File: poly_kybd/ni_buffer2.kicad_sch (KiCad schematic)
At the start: 2 parts, among them U12 SN74LVC1G126DBVR, U13 SN74LVC1G126DBVR

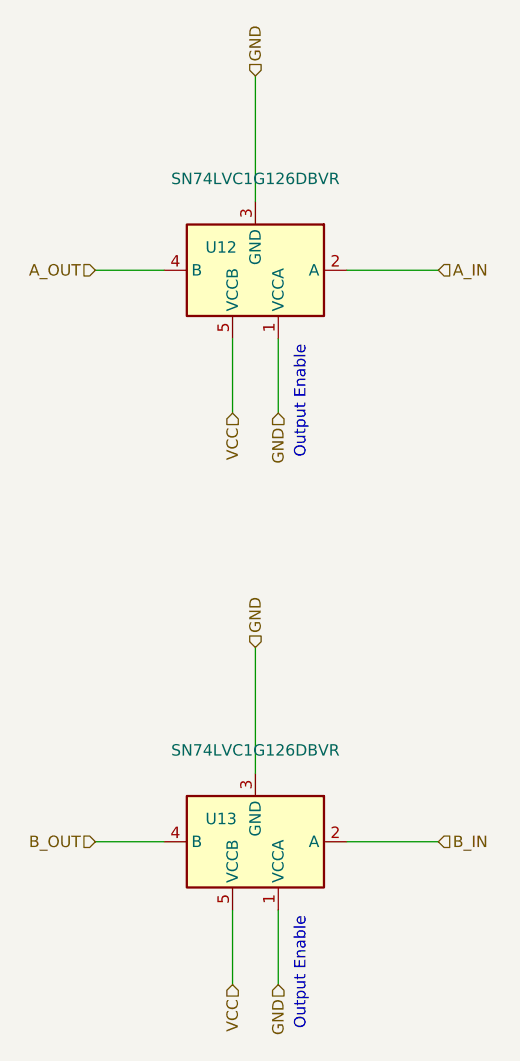
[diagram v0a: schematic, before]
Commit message: v3.3: replace SN74LVC1G126 buffer symbol with Nexperia 74AHC1G125
U12/U13 in ni_buffer2.kicad_sch were drawn with the
Logic_LevelTranslator:SN74AUP1T34DCK symbol, which mislabels pins 1 and 5
as VCCA/VCCB. The fitted part is a single-gate tri-state buffer, where
pin 1 is /OE and pin 5 is VCC.

Pin *numbers* drive the netlist and those were always right, so the built
v3.2 boards are electrically correct. This is a drawing fix - it matters
because the schematic is exported into the CE technical file.

- swap to 74xGxx:74AHC1G125, rev v3.3
- retarget U12/U13 to Nexperia 74AHC1G125GW,125 (LCSC C85397); the
  previously specified part is EOL at JLCPCB
- reroute the wires: the new symbol has different pin geometry, so all
  ten pins had to be reconnected. Net assignment verified unchanged -
  /OE and GND to GND, A to A_IN/B_IN, Y to A_OUT/B_OUT, VCC to VCC
- delete ni_buffer.kicad_sch and mini-360.kicad_sch, neither instantiated
  by any sheet

poly_kybd_split72_left.kicad_sch was rewritten from KiCad 8 to 9 format
on open. Verified harmless: all 186 symbol pins sit at identical
coordinates before and after. Note this is one-way - KiCad 8 can no
longer open the project.

The PCB still carries the old footprint value; Update PCB from Schematic
is the next step.

Co-Authored-By: Claude Opus 5 <noreply@anthropic.com>
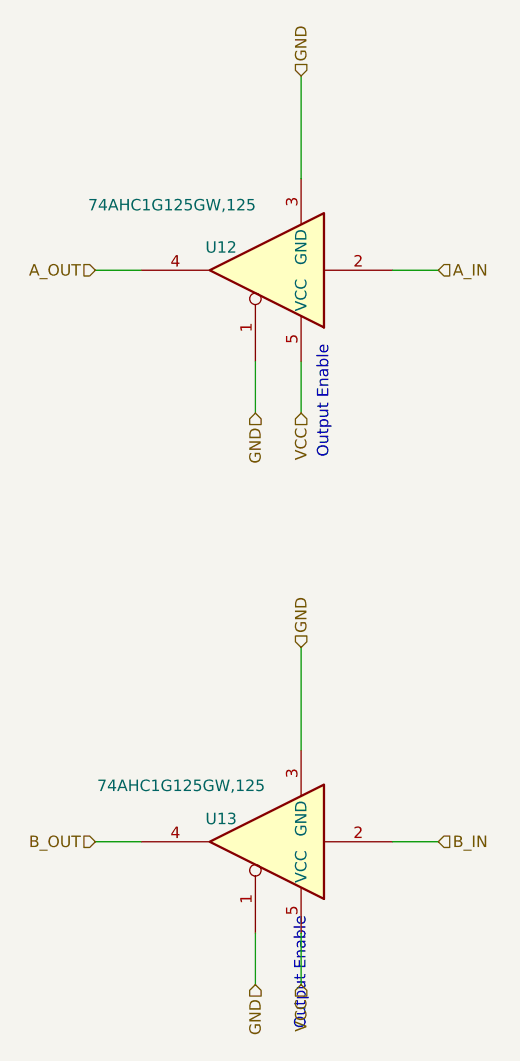
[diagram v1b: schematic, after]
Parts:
- U12, U13: value SN74LVC1G126DBVR -> 74AHC1G125GW,125; symbol Logic_LevelTranslator:SN74AUP1T34DCK -> 74xGxx:74AHC1G125; JLC C151890 -> C85397; LCSC C151890 -> C85397; MPN C151890 -> 74AHC1G125GW,125
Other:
- title: (none) -> Non Inverting Buffer
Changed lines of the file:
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@@
 	(generator_version "9.0")
 	(paper "A4")
+	(title_block
+		(title "Non Inverting Buffer")
+		(date "2026-08-06")
+		(rev "v3.3")
+	)
 	(text "Output Enable"
 		(exclude_from_sim no)
@@
 	(text "Output Enable"
 		(exclude_from_sim no)
-		(at 142.24 92.71 90)
+		(at 144.78 92.71 90)
 		(effects
 			(font
@@
 	(wire
 		(pts
-			(xy 136.525 50.165) (xy 136.525 64.135)
-		)
-		(stroke
-			(width 0)
-			(type default)
-		)
-	)
-	(wire
-		(pts
-			(xy 139.065 79.375) (xy 139.065 87.63)
-		)
-		(stroke
-			(width 0)
-			(type default)
-		)
-	)
-	(wire
-		(pts
-			(xy 139.065 142.875) (xy 139.065 151.13)
-		)
-		(stroke
-			(width 0)
-			(type default)
-		)
-	)
-	(wire
-		(pts
-			(xy 118.745 71.755) (xy 126.365 71.755)
-		)
-		(stroke
-			(width 0)
-			(type default)
-		)
-	)
-	(wire
-		(pts
-			(xy 133.985 142.875) (xy 133.985 151.13)
-		)
-		(stroke
-			(width 0)
-			(type default)
-		)
-	)
-	(wire
-		(pts
-			(xy 133.985 79.375) (xy 133.985 87.63)
-		)
-		(stroke
-			(width 0)
-			(type default)
-		)
-	)
-	(wire
-		(pts
-			(xy 136.525 113.665) (xy 136.525 127.635)
-		)
-		(stroke
-			(width 0)
-			(type default)
-		)
-	)
-	(wire
-		(pts
-			(xy 118.745 135.255) (xy 126.365 135.255)
-		)
-		(stroke
-			(width 0)
-			(type default)
-		)
-	)
-	(wire
-		(pts
-			(xy 146.685 71.755) (xy 156.845 71.755)
-		)
-		(stroke
-			(width 0)
-			(type default)
-		)
-	)
-	(wire
-		(pts
-			(xy 146.685 135.255) (xy 156.845 135.255)
-		)
-		(stroke
-			(width 0)
-			(type default)
+			(xy 118.745 71.755) (xy 123.825 71.755)
+		)
+		(stroke
+			(width 0)
+			(type default)
+		)
+	)
+	(wire
+		(pts
+			(xy 156.845 71.755) (xy 151.765 71.755)
+		)
+		(stroke
+			(width 0)
+			(type default)
+		)
+	)
+	(wire
+		(pts
+			(xy 141.605 50.165) (xy 141.605 61.595)
+		)
+		(stroke
+			(width 0)
+			(type default)
+		)
+	)
+	(wire
+		(pts
+			(xy 136.525 87.63) (xy 136.525 81.915)
+		)
+		(stroke
+			(width 0)
+			(type default)
+		)
+	)
+	(wire
+		(pts
+			(xy 141.605 113.665) (xy 141.605 125.095)
+		)
+		(stroke
+			(width 0)
+			(type default)
+		)
+	)
+	(wire
+		(pts
+			(xy 156.845 135.255) (xy 151.765 135.255)
+		)
+		(stroke
+			(width 0)
+			(type default)
+		)
+	)
+	(wire
+		(pts
+			(xy 141.605 151.13) (xy 141.605 145.415)
+		)
+		(stroke
+			(width 0)
+			(type default)
+		)
+	)
+	(wire
+		(pts
+			(xy 141.605 87.63) (xy 141.605 81.915)
+		)
+		(stroke
+			(width 0)
+			(type default)
+		)
+	)
+	(wire
+		(pts
+			(xy 118.745 135.255) (xy 123.825 135.255)
+		)
+		(stroke
+			(width 0)
+			(type default)
+		)
+	)
+	(wire
+		(pts
+			(xy 136.525 151.13) (xy 136.525 145.415)
+		)
+		(stroke
+			(width 0)
+			(type default)
+		)
+	)
+	(hierarchical_label "VCC"
+		(shape input)
+		(at 141.605 151.13 270)
+		(effects
+			(font
+				(size 1.27 1.27)
+			)
+			(justify right)
+		)
+	)
+	(hierarchical_label "B_OUT"
+		(shape input)
+		(at 118.745 135.255 180)
+		(effects
+			(font
+				(size 1.27 1.27)
+			)
+			(justify right)
+		)
+	)
+	(hierarchical_label "A_OUT"
+		(shape input)
+		(at 118.745 71.755 180)
+		(effects
+			(font
+				(size 1.27 1.27)
+			)
+			(justify right)
 		)
 	)
 	(hierarchical_label "GND"
 		(shape input)
-		(at 139.065 151.13 270)
-		(effects
-			(font
-				(size 1.27 1.27)
-			)
-			(justify right)
-		)
-	)
-	(hierarchical_label "B_OUT"
-		(shape input)
-		(at 118.745 135.255 180)
-		(effects
-			(font
-				(size 1.27 1.27)
-			)
-			(justify right)
-		)
-	)
-	(hierarchical_label "A_OUT"
-		(shape input)
-		(at 118.745 71.755 180)
-		(effects
-			(font
-				(size 1.27 1.27)
-			)
-			(justify right)
+		(at 141.605 50.165 90)
+		(effects
+			(font
+				(size 1.27 1.27)
+			)
+			(justify left)
 		)
 	)
 	(hierarchical_label "GND"
 		(shape input)
-		(at 136.525 50.165 90)
+		(at 136.525 87.63 270)
+		(effects
+			(font
+				(size 1.27 1.27)
+			)
+			(justify right)
+		)
+	)
+	(hierarchical_label "B_IN"
+		(shape input)
+		(at 156.845 135.255 0)
 		(effects
 			(font
@@
 	(hierarchical_label "VCC"
 		(shape input)
-		(at 133.985 87.63 270)
-		(effects
-			(font
-				(size 1.27 1.27)
-			)
-			(justify right)
-		)
-	)
-	(hierarchical_label "B_IN"
-		(shape input)
-		(at 156.845 135.255 0)
+		(at 141.605 87.63 270)
+		(effects
+			(font
+				(size 1.27 1.27)
+			)
+			(justify right)
+		)
+	)
+	(hierarchical_label "GND"
+		(shape input)
+		(at 141.605 113.665 90)
 		(effects
 			(font
@@
 	(hierarchical_label "GND"
 		(shape input)
-		(at 139.065 87.63 270)
-		(effects
-			(font
-				(size 1.27 1.27)
-			)
-			(justify right)
-		)
-	)
-	(hierarchical_label "GND"
-		(shape input)
-		(at 136.525 113.665 90)
+		(at 136.525 151.13 270)
+		(effects
+			(font
+				(size 1.27 1.27)
+			)
+			(justify right)
+		)
+	)
+	(hierarchical_label "A_IN"
+		(shape input)
+		(at 156.845 71.755 0)
 		(effects
 			(font
@@
 		)
 	)
-	(hierarchical_label "VCC"
-		(shape input)
-		(at 133.985 151.13 270)
-		(effects
-			(font
-				(size 1.27 1.27)
-			)
-			(justify right)
-		)
-	)
-	(hierarchical_label "A_IN"
-		(shape input)
-		(at 156.845 71.755 0)
-		(effects
-			(font
-				(size 1.27 1.27)
-			)
-			(justify left)
-		)
-	)
 	(symbol
-		(lib_id "Logic_LevelTranslator:SN74AUP1T34DCK")
+		(lib_id "74xGxx:74AHC1G125")
 		(at 136.525 71.755 180)
 		(unit 1)
@@
 			)
 		)
-		(property "Value" "SN74LVC1G126DBVR"
-			(at 136.525 61.595 0)
+		(property "Value" "74AHC1G125GW,125"
+			(at 127.254 64.516 0)
 			(effects
 				(font
@@
 			)
 		)
-		(property "Datasheet" "https://www.ti.com/cn/lit/gpn/sn74ahc1g125"
+		(property "Datasheet" "https://assets.nexperia.com/documents/data-sheet/74AHC_AHCT1G125.pdf"
 			(at 136.525 56.515 0)
 			(effects
@@
 			)
 		)
-		(property "MPN" "C151890"
-			(at 136.525 71.755 0)
-			(effects
-				(font
-					(size 1.27 1.27)
-				)
-				(hide yes)
-			)
-		)
-		(property "JLC" "C151890"
-			(at 136.525 71.755 0)
-			(effects
-				(font
-					(size 1.27 1.27)
-				)
-				(hide yes)
-			)
-		)
-		(property "LCSC" "C151890"
+		(property "MPN" "74AHC1G125GW,125"
+			(at 136.525 71.755 0)
+			(effects
+				(font
+					(size 1.27 1.27)
+				)
+				(hide yes)
+			)
+		)
+		(property "JLC" "C85397"
+			(at 136.525 71.755 0)
+			(effects
+				(font
+					(size 1.27 1.27)
+				)
+				(hide yes)
+			)
+		)
+		(property "LCSC" "C85397"
 			(at 136.525 71.755 0)
 			(effects
@@
 	)
 	(symbol
-		(lib_id "Logic_LevelTranslator:SN74AUP1T34DCK")
+		(lib_id "74xGxx:74AHC1G125")
 		(at 136.525 135.255 180)
 		(unit 1)
@@
 			)
 		)
-		(property "Value" "SN74LVC1G126DBVR"
-			(at 136.525 125.095 0)
+		(property "Value" "74AHC1G125GW,125"
+			(at 128.27 129.032 0)
 			(effects
 				(font
@@
 			)
 		)
-		(property "Datasheet" "https://www.ti.com/cn/lit/gpn/sn74ahc1g125"
+		(property "Datasheet" "https://assets.nexperia.com/documents/data-sheet/74AHC_AHCT1G125.pdf"
 			(at 136.525 120.015 0)
 			(effects
@@
 			)
 		)
-		(property "MPN" "C151890"
+		(property "MPN" "74AHC1G125GW,125"
 			(at 136.525 135.255 0)
 			(effects
@@
 			)
 		)
-		(property "JLC" "C151890"
+		(property "JLC" "C85397"
 			(at 136.525 135.255 0)
 			(effects
@@
 			)
 		)
-		(property "LCSC" "C151890"
+		(property "LCSC" "C85397"
 			(at 136.525 135.255 0)
 			(effects

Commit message: U12/U13: correct Manufacturer field to Nexperia
Missed in the v3.3 symbol swap (#23). The part was retargeted from the
EOL TI/TECH PUBLIC C151890 to Nexperia 74AHC1G125GW,125 (C85397), and
Value, Datasheet, MPN, JLC and LCSC were all updated - but Manufacturer
was left reading "TI".

This matters before Update PCB from Schematic, because the field
propagates to the footprint and into the CE parts list. "Nexperia" is
already the spelling used elsewhere in the project.

RoHS stays "x" and Description stays empty, matching the convention used
across the other sheets.

Co-Authored-By: Claude Opus 5 <noreply@anthropic.com>
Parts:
- U12, U13: Manufacturer TI -> Nexperia
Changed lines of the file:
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@@
 			)
 		)
-		(property "Manufacturer" "TI"
+		(property "Manufacturer" "Nexperia"
 			(at 136.525 71.755 0)
 			(effects
@@
 			)
 		)
-		(property "Manufacturer" "TI"
+		(property "Manufacturer" "Nexperia"
 			(at 136.525 135.255 0)
 			(effects
